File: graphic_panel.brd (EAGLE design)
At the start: 128.5 x 30 mm, 10 parts

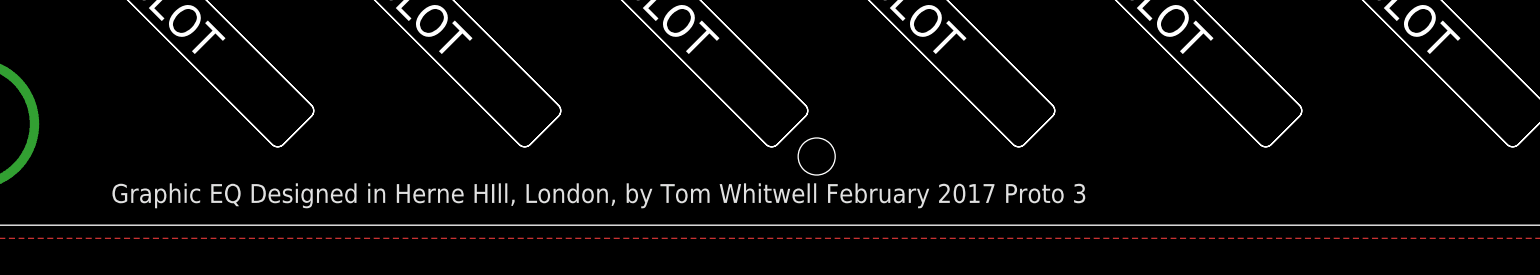
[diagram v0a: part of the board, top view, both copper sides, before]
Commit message: Revision 1 board finalised - moved one resistor + added Fiducials
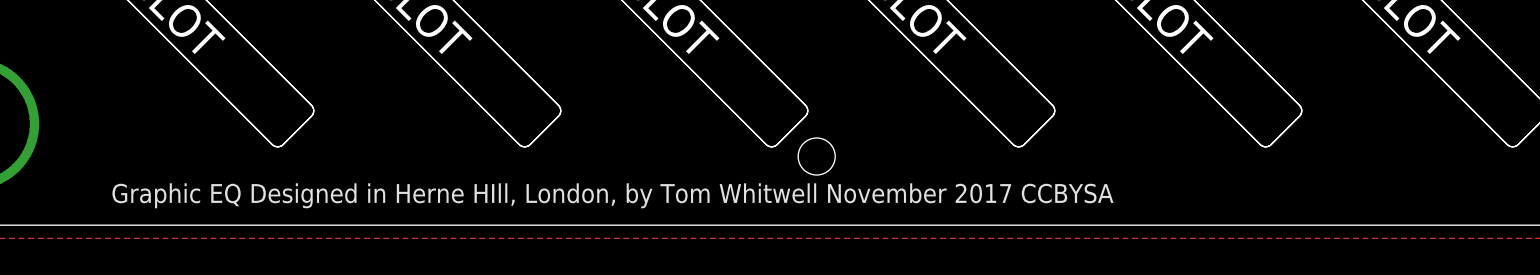
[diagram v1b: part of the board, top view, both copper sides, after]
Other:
- board text added: "Graphic EQ Designed in Herne HIll, London, by Tom Whitwell November 2017 CCBYSA"
- board text removed: "Graphic EQ Designed in Herne HIll, London, by Tom Whitwell February 2017 Proto 3"
